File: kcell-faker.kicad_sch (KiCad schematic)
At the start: 27 parts, among them J4 DBG, SW1 BOOT, SW2 RST, SW3 UP, SW4 DOWN, SW5 RANGE, U6 ESP32-S3-MINI-1

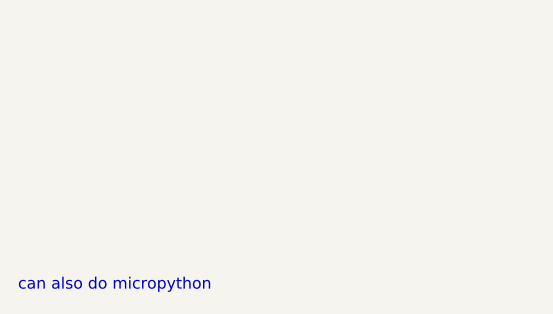
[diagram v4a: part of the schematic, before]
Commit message: update to match library changes, update to include repo
After moving all in house, label the board with a correct internal url
Updated the library to have new "LCSC Part #" instead of "LCSC Part#"
and updated all symbols to match that.  Updated to the neweer standard
14/16 pin usb connector symbols

_should_ be final for gerbesr
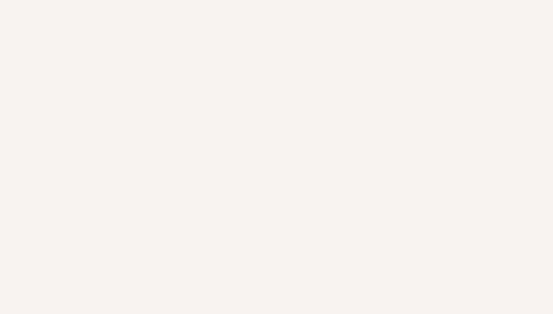
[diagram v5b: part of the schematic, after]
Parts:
- C1, C3: LCSC Part # (none) -> C15850
- C10, C11, C14, C6, C7, C8: LCSC Part # (none) -> C14663
- C9: LCSC Part # (none) -> C15849
- R12, R13: LCSC Part # (none) -> C23138
- R19: LCSC Part # (none) -> C23193
- R20, R22: LCSC Part # (none) -> C25804
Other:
- note removed: "can also do micropython"
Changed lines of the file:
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@@
 		)
 	)
-	(text "can also do micropython"
-		(exclude_from_sim no)
-		(at -31.242 208.534 0)
-		(effects
-			(font
-				(size 1.27 1.27)
-			)
-			(justify left)
-		)
-	)
 	(text "Manual Controls\nRange button toggles coarse/fine digipot\nUp/down just \"up/down\" the spi value for the appropriate range\nGreen LED: which range is in use\nRed LED: ....? current range value has hit a limit?"
 		(exclude_from_sim no)
@@
 			)
 		)
+		(property "LCSC Part #" "C14663"
+			(at 129.54 186.69 0)
+			(effects
+				(font
+					(size 1.27 1.27)
+				)
+				(hide yes)
+			)
+		)
 		(pin "2"
 		)
@@
 			)
 		)
+		(property "LCSC Part #" "C23138"
+			(at 35.56 177.8 0)
+			(effects
+				(font
+					(size 1.27 1.27)
+				)
+				(hide yes)
+			)
+		)
 		(pin "1"
 		)
@@
 			)
 		)
+		(property "LCSC Part #" "C14663"
+			(at 160.02 74.93 0)
+			(effects
+				(font
+					(size 1.27 1.27)
+				)
+				(hide yes)
+			)
+		)
 		(pin "2"
 		)
@@
 			)
 		)
+		(property "LCSC Part #" "C14663"
+			(at 81.28 186.69 0)
+			(effects
+				(font
+					(size 1.27 1.27)
+				)
+				(hide yes)
+			)
+		)
 		(pin "2"
 		)
@@
 			)
 		)
+		(property "LCSC Part #" "C15849"
+			(at 195.58 71.12 0)
+			(effects
+				(font
+					(size 1.27 1.27)
+				)
+				(hide yes)
+			)
+		)
 		(pin "2"
 		)
@@
 			)
 		)
+		(property "LCSC Part #" "C25804"
+			(at 55.88 43.18 0)
+			(effects
+				(font
+					(size 1.27 1.27)
+				)
+				(hide yes)
+			)
+		)
 		(pin "2"
 		)
@@
 			)
 		)
+		(property "LCSC Part #" "C15850"
+			(at 165.1 34.29 0)
+			(effects
+				(font
+					(size 1.27 1.27)
+				)
+				(hide yes)
+			)
+		)
 		(pin "2"
 		)
@@
 			)
 		)
+		(property "LCSC Part #" "C14663"
+			(at 104.14 186.69 0)
+			(effects
+				(font
+					(size 1.27 1.27)
+				)
+				(hide yes)
+			)
+		)
 		(pin "2"
 		)
@@
 			)
 		)
+		(property "LCSC Part #" "C25804"
+			(at 55.88 40.64 0)
+			(effects
+				(font
+					(size 1.27 1.27)
+				)
+				(hide yes)
+			)
+		)
 		(pin "2"
 		)
@@
 			)
 		)
+		(property "LCSC Part #" "C23193"
+			(at 109.22 30.48 0)
+			(effects
+				(font
+					(size 1.27 1.27)
+				)
+				(hide yes)
+			)
+		)
 		(pin "2"
 		)
@@
 			)
 		)
+		(property "LCSC Part #" "C14663"
+			(at 144.78 34.29 0)
+			(effects
+				(font
+					(size 1.27 1.27)
+				)
+				(hide yes)
+			)
+		)
 		(pin "2"
 		)
@@
 			)
 		)
+		(property "LCSC Part #" "C14663"
+			(at 182.88 74.93 0)
+			(effects
+				(font
+					(size 1.27 1.27)
+				)
+				(hide yes)
+			)
+		)
 		(pin "2"
 		)
@@
 			)
 		)
+		(property "LCSC Part #" "C15850"
+			(at 154.94 34.29 0)
+			(effects
+				(font
+					(size 1.27 1.27)
+				)
+				(hide yes)
+			)
+		)
 		(pin "2"
 		)
@@
 			(at 48.26 177.8 0)
 			(effects
+				(font
+					(size 1.27 1.27)
+				)
+				(hide yes)
+			)
+		)
+		(property "LCSC Part #" "C23138"
+			(at 48.26 177.8 0)
+			(effects

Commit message: yet more part number syncing
Because parts go to pcb as well, lots more syncing ws needed. hopefully
this will be more streamlined in future
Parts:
- D1: LCSC Part # (none) -> C84256
- D3: LCSC Part # (none) -> C2297
- J4: LCSC Part # (none) -> C2937625
- R22: jlcbasic (none) -> basic
- R9: LCSC Part # (none) -> C25804
- SW1, SW2, SW3, SW4, SW5: LCSC Part # (none) -> C318884
- U6: LCSC Part # (none) -> C2913206
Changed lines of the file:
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@@
+			)
+		)
+		(property "LCSC Part #" "C2913206"
+			(at 86.36 55.88 0)
+			(effects
+				(font
+					(size 1.27 1.27)
+				)
+				(hide yes)
 			)
 		)
@@
 			)
 		)
+		(property "LCSC Part #" "C318884"
+			(at 99.06 177.8 0)
+			(effects
+				(font
+					(size 1.27 1.27)
+				)
+				(hide yes)
+			)
+		)
 		(pin "1"
 		)
@@
 		)
 		(property "LCSC Part #" "C25804"
+			(at 55.88 43.18 0)
+			(effects
+				(font
+					(size 1.27 1.27)
+				)
+				(hide yes)
+			)
+		)
+		(property "jlcbasic" "basic"
 			(at 55.88 43.18 0)
 			(effects
@@
 			)
 		)
+		(property "LCSC Part #" "C318884"
+			(at 177.8 66.04 0)
+			(effects
+				(font
+					(size 1.27 1.27)
+				)
+				(hide yes)
+			)
+		)
 		(pin "1"
 		)
@@
 			)
 		)
+		(property "LCSC Part #" "C2297"
+			(at 35.56 170.18 0)
+			(effects
+				(font
+					(size 1.27 1.27)
+				)
+				(hide yes)
+			)
+		)
 		(pin "1"
 		)
@@
 			)
 		)
+		(property "LCSC Part #" "C25804"
+			(at 195.58 60.96 0)
+			(effects
+				(font
+					(size 1.27 1.27)
+				)
+				(hide yes)
+			)
+		)
 		(pin "1"
 		)
@@
 			)
 		)
+		(property "LCSC Part #" "C318884"
+			(at 76.2 177.8 0)
+			(effects
+				(font
+					(size 1.27 1.27)
+				)
+				(hide yes)
+			)
+		)
 		(pin "1"
 		)
@@
 			)
 		)
+		(property "LCSC Part #" "C84256"
+			(at 48.26 170.18 0)
+			(effects
+				(font
+					(size 1.27 1.27)
+				)
+				(hide yes)
+			)
+		)
 		(pin "1"
 		)
@@
 			)
 		)
+		(property "LCSC Part #" "C2937625"
+			(at 129.54 33.02 0)
+			(effects
+				(font
+					(size 1.27 1.27)
+				)
+				(hide yes)
+			)
+		)
 		(pin "3"
 		)
@@
 			)
 		)
+		(property "LCSC Part #" "C318884"
+			(at 154.94 66.04 0)
+			(effects
+				(font
+					(size 1.27 1.27)
+				)
+				(hide yes)
+			)
+		)
 		(pin "1"
 		)
@@
 			(at 124.46 177.8 0)
 			(effects
+				(font
+					(size 1.27 1.27)
+				)
+				(hide yes)
+			)
+		)
+		(property "LCSC Part #" "C318884"
+			(at 124.46 177.8 0)
+			(effects
